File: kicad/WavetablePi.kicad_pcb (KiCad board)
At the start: 2 copper layers, 39 x 75.7 mm, 9 parts

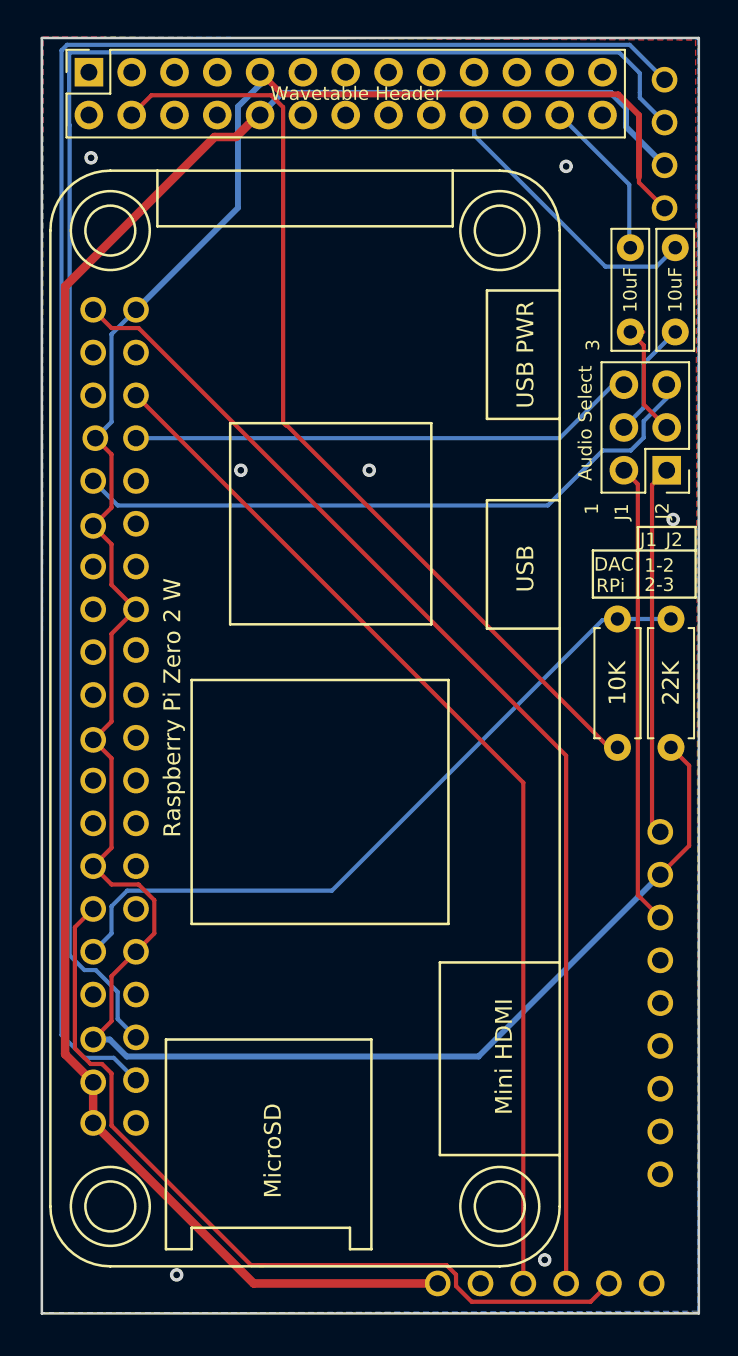
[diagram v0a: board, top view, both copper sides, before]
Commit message: Adds a low-pass filter for PWM audio
Improves the audio quality of PWM audio with a simple low-pass filter.
This uses R3-C3 and R4-C4 (one filter for each channel).
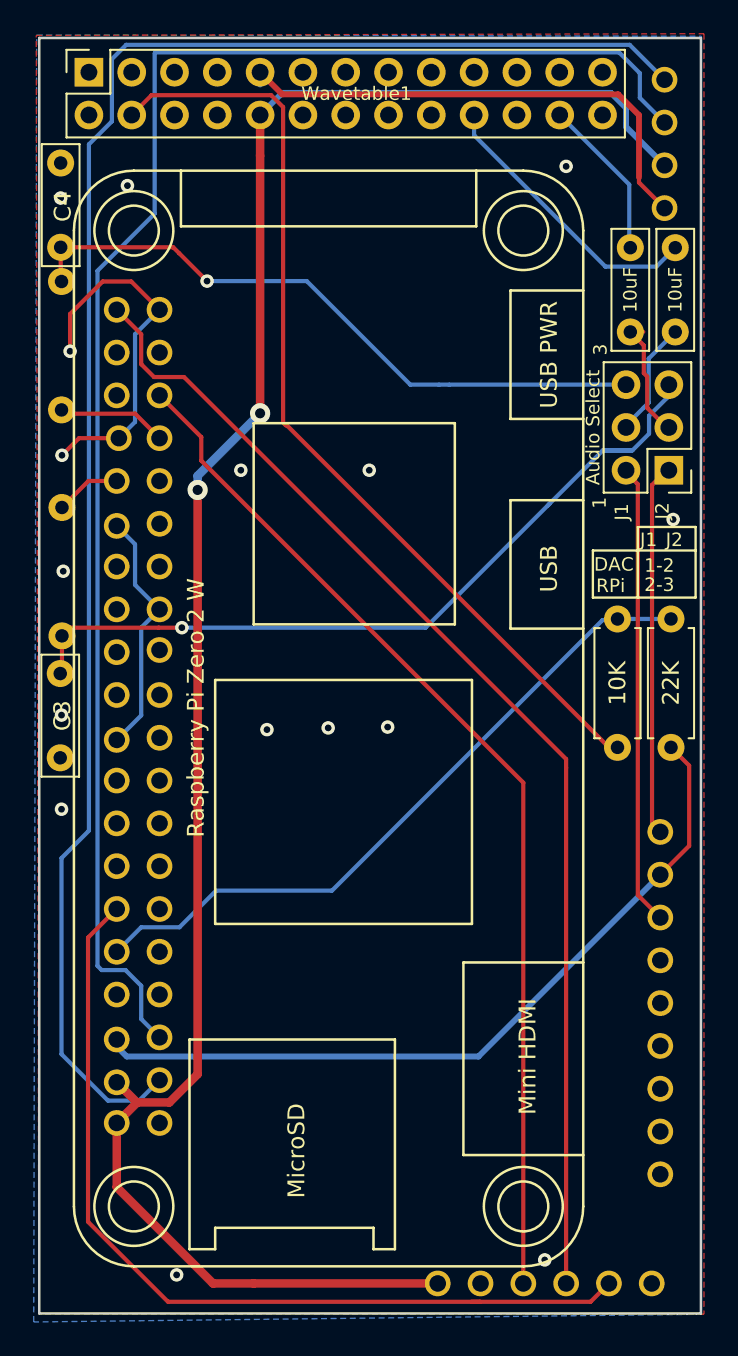
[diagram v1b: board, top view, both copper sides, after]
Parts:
- added C3: 100nF, Capacitor_THT:C_Rect_L7.0mm_W2.0mm_P5.00mm, F.Cu at (120.3, 51.9)
- added C4: C, Capacitor_THT:C_Rect_L7.0mm_W2.0mm_P5.00mm, F.Cu at (120.4, 26.6)
- added R3: 1K, Resistor_THT:R_Axial_DIN0207_L6.3mm_D2.5mm_P7.62mm_Horizontal, B.Cu at (120.4, 49.7)
- added R4: 1K, Resistor_THT:R_Axial_DIN0207_L6.3mm_D2.5mm_P7.62mm_Horizontal, B.Cu at (120.4, 28.7)
- Wavetable1: renamed from Wavetable Header
- moved Raspberry Pi Zero 2 W 1.40 mm to (121.2, 87.1)
- moved Audio Select 0.13 mm to (156.5, 39.9)
- renumbered DAC to DAC1, Display to LCD1
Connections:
- DAC1 pad 1: Net-(DAC1-Pad1) -> (no net)
- DAC1 pad 10: Net-(DAC1-Pad10) -> (no net)
- DAC1 pad 11: Net-(DAC1-Pad11) -> (no net)
- DAC1 pad 12: Net-(DAC1-Pad12) -> (no net)
- DAC1 pad 7: Net-(DAC1-Pad7) -> (no net)
- DAC1 pad 8: Net-(DAC1-Pad8) -> (no net)
- DAC1 pad 9: Net-(DAC1-Pad9) -> (no net)
- Raspberry Pi Zero 2 W pad 1: Net-(RPi1-Pad1) -> (no net)
- Raspberry Pi Zero 2 W pad 17: Net-(RPi1-Pad17) -> (no net)
- Raspberry Pi Zero 2 W pad 18: Net-(RPi1-Pad18) -> (no net)
- Raspberry Pi Zero 2 W pad 19: Net-(RPi1-Pad19) -> (no net)
- Raspberry Pi Zero 2 W pad 21: Net-(RPi1-Pad21) -> (no net)
- Raspberry Pi Zero 2 W pad 22: Net-(RPi1-Pad22) -> (no net)
- Raspberry Pi Zero 2 W pad 23: Net-(RPi1-Pad23) -> (no net)
- Raspberry Pi Zero 2 W pad 24: Net-(RPi1-Pad24) -> (no net)
- Raspberry Pi Zero 2 W pad 26: Net-(RPi1-Pad26) -> (no net)
- Raspberry Pi Zero 2 W pad 27: Net-(RPi1-Pad27) -> (no net)
- Raspberry Pi Zero 2 W pad 28: Net-(RPi1-Pad28) -> (no net)
- Raspberry Pi Zero 2 W pad 29: Net-(RPi1-Pad29) -> (no net)
- Raspberry Pi Zero 2 W pad 31: Net-(RPi1-Pad31) -> (no net)
- Raspberry Pi Zero 2 W pad 32: Net-(Audio_Select1-Pad5) -> Net-(R3-Pad2)
- Raspberry Pi Zero 2 W pad 33: Net-(Audio_Select1-Pad6) -> Net-(R4-Pad2)
- Raspberry Pi Zero 2 W pad 36: Net-(RPi1-Pad36) -> (no net)
- Raspberry Pi Zero 2 W pad 37: Net-(RPi1-Pad37) -> (no net)
- Raspberry Pi Zero 2 W pad 38: Net-(RPi1-Pad38) -> (no net)
- Raspberry Pi Zero 2 W pad 7: Net-(RPi1-Pad7) -> (no net)
- Raspberry Pi Zero 2 W pad 8: Net-(RPi1-Pad8) -> (no net)
- Wavetable1 pad 1: Net-(Wavetable1-Pad1) -> GND
- Wavetable1 pad 11: Net-(Wavetable1-Pad11) -> (no net)
- Wavetable1 pad 12: Net-(Wavetable1-Pad12) -> (no net)
- Wavetable1 pad 13: Net-(Wavetable1-Pad13) -> (no net)
- Wavetable1 pad 14: Net-(Wavetable1-Pad14) -> (no net)
- Wavetable1 pad 15: Net-(Wavetable1-Pad15) -> (no net)
- Wavetable1 pad 16: Net-(Wavetable1-Pad16) -> (no net)
- Wavetable1 pad 17: Net-(Wavetable1-Pad17) -> (no net)
- Wavetable1 pad 18: Net-(Wavetable1-Pad18) -> (no net)
- Wavetable1 pad 19: Net-(Wavetable1-Pad19) -> (no net)
- Wavetable1 pad 2: Net-(Wavetable1-Pad2) -> (no net)
- Wavetable1 pad 21: Net-(Wavetable1-Pad21) -> (no net)
- Wavetable1 pad 22: Net-(Wavetable1-Pad22) -> (no net)
- Wavetable1 pad 23: Net-(Wavetable1-Pad23) -> (no net)
- Wavetable1 pad 25: Net-(Wavetable1-Pad25) -> (no net)
- Wavetable1 pad 26: Net-(Wavetable1-Pad26) -> (no net)
- Wavetable1 pad 3: Net-(Wavetable1-Pad3) -> (no net)
- Wavetable1 pad 5: Net-(Wavetable1-Pad5) -> (no net)
- Wavetable1 pad 6: Net-(Wavetable1-Pad6) -> (no net)
- Wavetable1 pad 7: Net-(Wavetable1-Pad7) -> (no net)
- Wavetable1 pad 8: Net-(Wavetable1-Pad8) -> (no net)
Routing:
- net GND: track 146.2 -> 113.0 mm, vias 7 -> 16
- net Net-(Audio_Select1-Pad5): track 38.6 -> 48.1 mm, vias 0 -> 1
- net Net-(Audio_Select1-Pad6): track 29.9 -> 39.2 mm, vias 0 -> 1
- net Net-(R4-Pad2): track 0.00 -> 6.51 mm
- net Net-(R3-Pad2): track 0.00 -> 3.90 mm
- net Net-(DAC1-Pad2): track 49.6 -> 53.1 mm
- net Net-(LCD1-Pad2): track 98.4 -> 95.0 mm
- net Net-(R1-Pad1): track 43.4 -> 41.1 mm
- net Net-(LCD1-Pad1): track 100.7 -> 101.8 mm
- net +5V: track 117.6 -> 118.5 mm, vias 0 -> 2
- net Net-(DAC1-Pad4): track 62.2 -> 61.6 mm
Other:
- board size 39 x 75.7 mm -> 39.3 x 75.7 mm
- board text added: "rev0.3"
- board text removed: "rev0.2"
